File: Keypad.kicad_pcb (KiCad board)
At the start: 2 copper layers, 119.9 x 118.6 mm, 78 parts, among them U1 TEENSY2.0

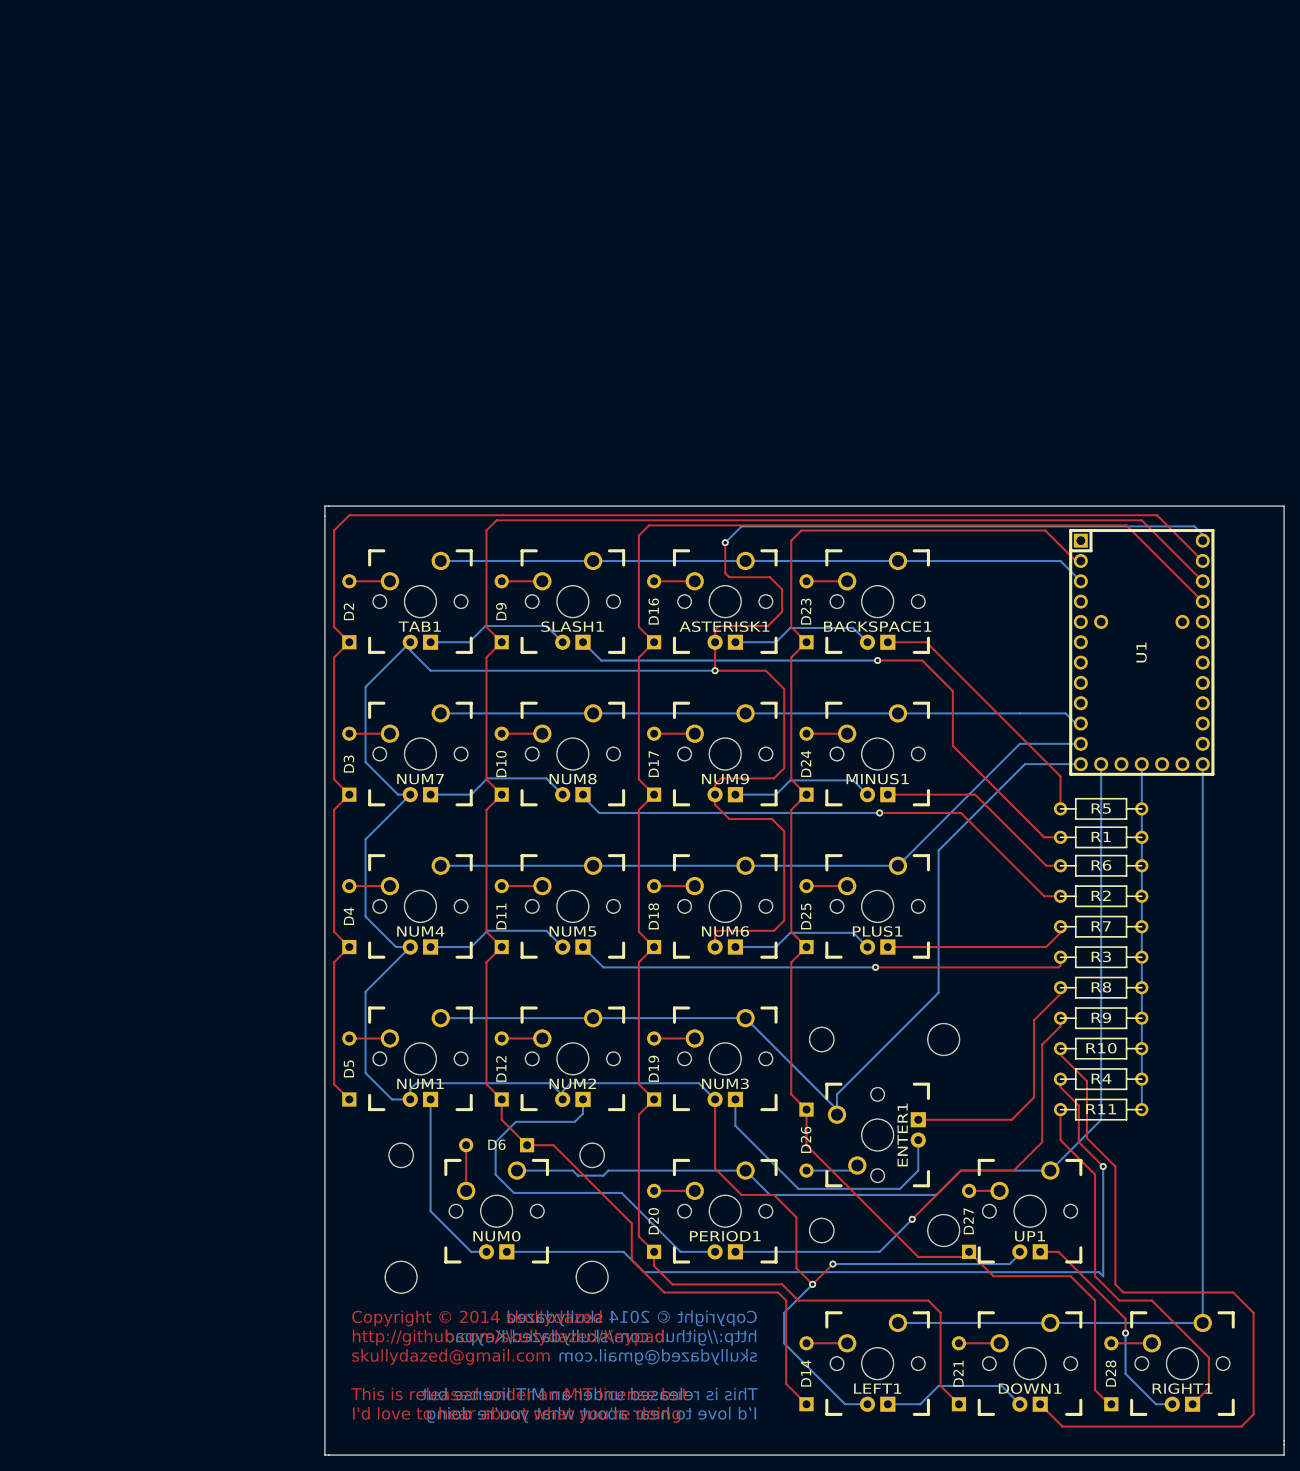
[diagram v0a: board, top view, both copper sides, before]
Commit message: Adding images so people can see what it looks like
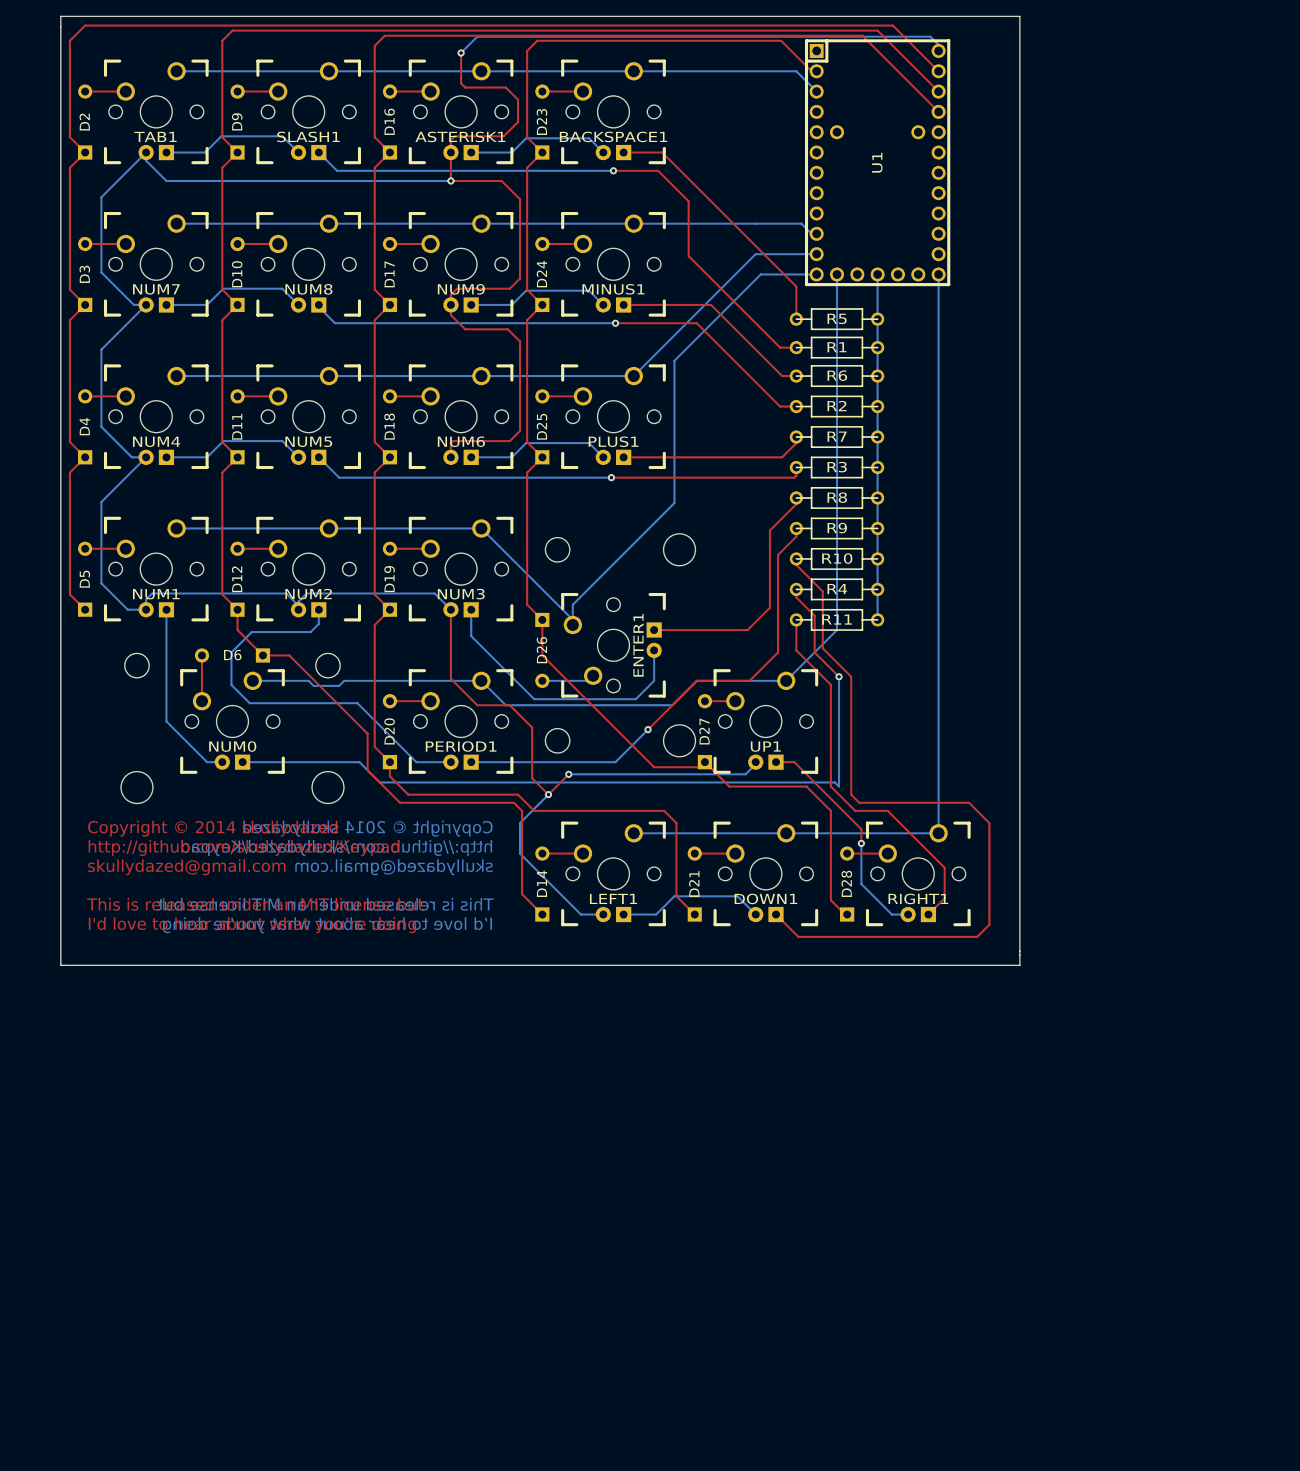
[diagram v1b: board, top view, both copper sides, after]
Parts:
- moved D14 69.6 mm to (78.5, 121.2)
- moved D21 69.6 mm to (97.5, 121.2)
- moved D26 69.6 mm to (68.3, 91.9)
- moved D28 69.6 mm to (116.6, 121.2)
- moved D6 69.6 mm to (34.7, 87.5)
- moved LED15 69.6 mm to (63.2, 81.8)
- moved LED17 69.6 mm to (44.2, 81.8)
- moved LED7 69.6 mm to (25.1, 81.8)
- moved NUM1 69.6 mm to (25.1, 81.8)
- moved NUM2 69.6 mm to (44.2, 81.8)
- moved NUM3 69.6 mm to (63.2, 81.8)
- moved R1 69.6 mm to (110.2, 54.1)
- moved R5 69.6 mm to (110.2, 50.5)
- moved ASTERISK1 69.6 mm to (63.2, 24.6)
- moved BACKSPACE1 69.6 mm to (82.3, 24.6)
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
